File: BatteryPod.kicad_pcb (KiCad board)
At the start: 2 copper layers, 71.5 x 86.6 mm, 15 parts, among them J1 Conn_01x02_Pin, U1 LM5157RTER

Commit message: feat: almost full initial routing
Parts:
- added C8: 100uF, Capacitor_SMD:CP_Elec_16x17.5, F.Cu at (112.2, 125.7)
- added H1: MountingHole, MountingHole:MountingHole_2.5mm, B.Cu at (84.5, 103.5)
- added H2: MountingHole, MountingHole:MountingHole_2.5mm, B.Cu at (133.2, 100.4)
- added H3: MountingHole, MountingHole:MountingHole_2.5mm, B.Cu at (81.3, 141.9)
- added H4: MountingHole, MountingHole:MountingHole_2.5mm, B.Cu at (140.4, 142.0)
- C2: footprint Capacitor_SMD:C_0603_1608Metric -> Capacitor_SMD:C_2220_5750Metric
- J1: value Conn_01x02_Pin -> VIN; footprint Connector_PinHeader_2.54mm:PinHeader_1x02_P2.54mm_Vertical -> Connector_Wire:SolderWire-1.5sqmm_1x02_P7.8mm_D1.7mm_OD3.9mm
- moved R4 71.7 mm to (110.2, 79.9)
- moved R3 68.8 mm to (116.8, 81.4), turned to 180 degrees
- moved C6 64.6 mm to (113.1, 79.9), turned to 180 degrees
- moved C7 63.1 mm to (111.3, 83.7), turned to 180 degrees
- moved C5 60.7 mm to (113.1, 81.4), turned to 180 degrees
- moved U1 55.1 mm to (115.0, 84.3), turned to 180 degrees
- moved C3 54.4 mm to (118.7, 84.2), turned to 180 degrees
- moved R2 54.4 mm to (110.2, 82.2)
- moved J1 52.6 mm to (98.0, 82.0), turned to 135 degrees
- moved C2 51.2 mm to (91.5, 83.4), turned to 135 degrees
- moved R1 51.2 mm to (107.2, 82.2)
- moved C4 50.9 mm to (123.5, 92.4)
- moved D1 47.0 mm to (117.0, 89.8), turned to 180 degrees
- moved C1 41.9 mm to (122.0, 96.1)
- moved L1 11.4 mm to (104.0, 103.4), turned to 180 degrees
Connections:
- net Net-(D1-K) renamed VCC
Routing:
- net +BATT: track 0.00 -> 29.4 mm, vias 0 -> 1
- net VCC: track 0.00 -> 12.0 mm, vias 0 -> 2
- net /FB: track 0.00 -> 6.05 mm
- net Net-(U1-COMP): track 0.00 -> 3.04 mm
- net Net-(U1-SS): track 0.00 -> 1.76 mm
- net Net-(U1-VCC): track 0.00 -> 1.56 mm
- net Net-(U1-RT): track 0.00 -> 1.51 mm
- net Net-(C6-Pad2): track 0.00 -> 1.38 mm
- net GND: vias 0 -> 105
- added copper zone on F.Cu, net +BATT
- added copper zone on F.Cu, net /SW
- added copper zone on B.Cu, net GND
- added copper zone on F.Cu, net GND
- added copper zone on F.Cu, net VCC
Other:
- outline, holes or cut-outs redrawn
- board text added: "JLCJLCJLCJLC"

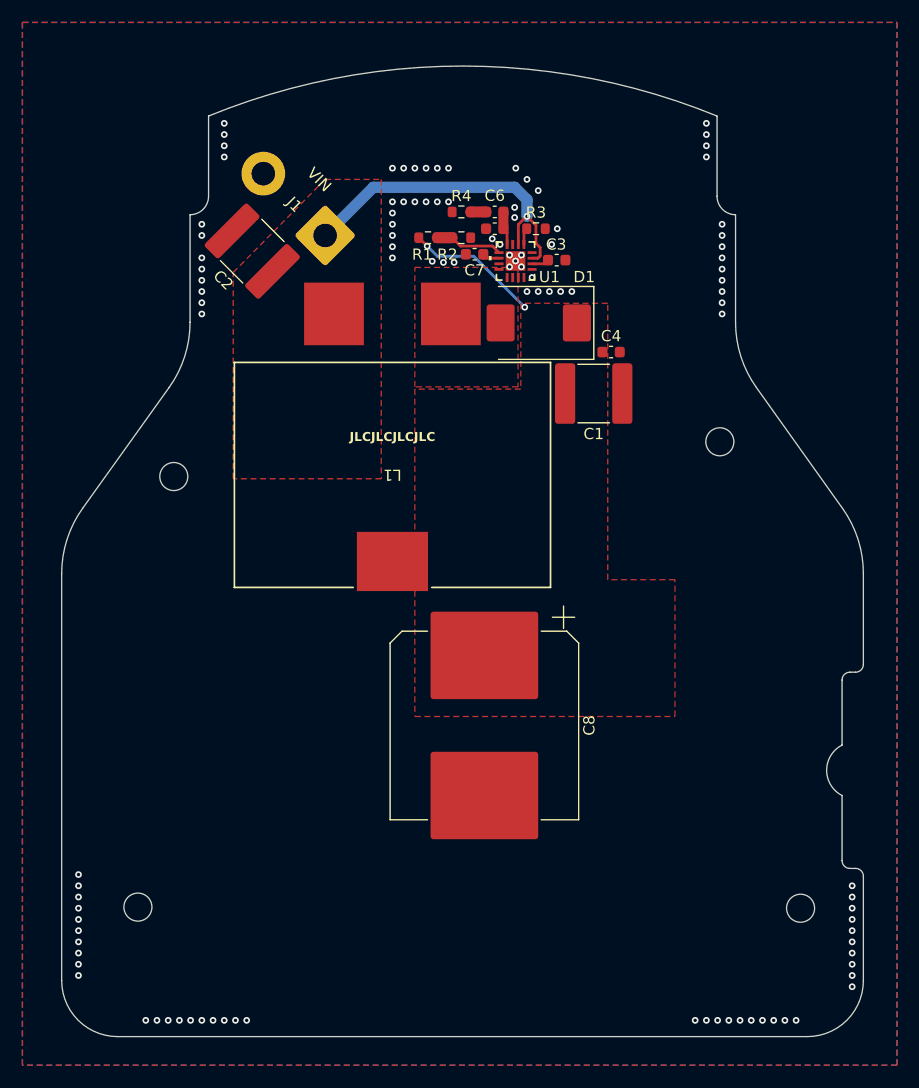
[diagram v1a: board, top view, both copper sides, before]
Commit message: feat: correct screw positioning (hopefully)
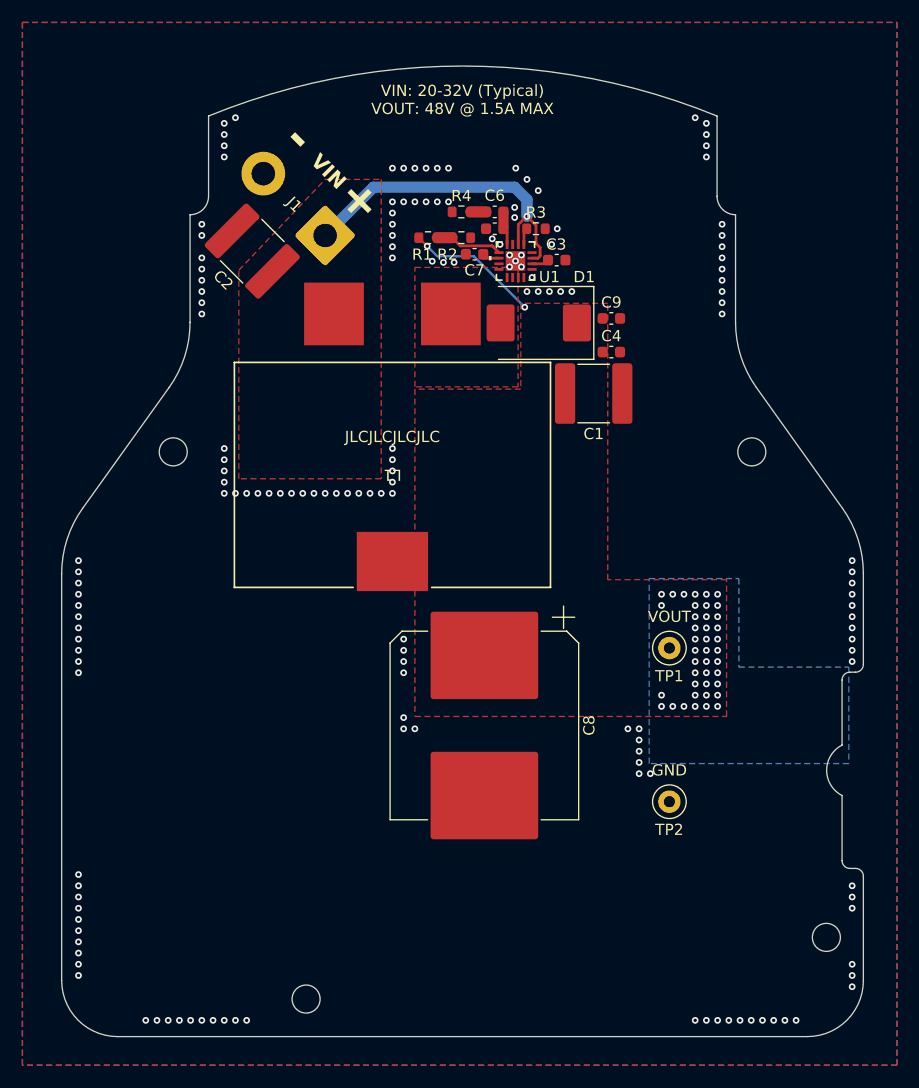
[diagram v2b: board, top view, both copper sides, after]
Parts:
- added C9: 0.1uF, Capacitor_SMD:C_0603_1608Metric, F.Cu at (123.5, 89.4)
- added TP1: VOUT, TestPoint:TestPoint_Loop_D2.50mm_Drill1.0mm_LowProfile, F.Cu at (128.7, 118.8)
- added TP2: GND, TestPoint:TestPoint_Loop_D2.50mm_Drill1.0mm_LowProfile, F.Cu at (128.7, 132.5)
- moved H3 17.1 mm to (96.3, 150.1)
- moved H4 3.47 mm to (142.7, 144.6)
- moved H2 2.99 mm to (136.1, 101.3)
- moved H1 2.20 mm to (84.5, 101.3)
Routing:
- net VCC: vias 2 -> 43
- net GND: vias 105 -> 162
- added copper zone on B.Cu, net VCC
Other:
- board text added: "+"
- board text added: "-"
- board text added: "VIN: 20-32V (Typical) VOUT: 48V @ 1.5A MAX"

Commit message: patch: silkscreen improvements fix: screw hole position
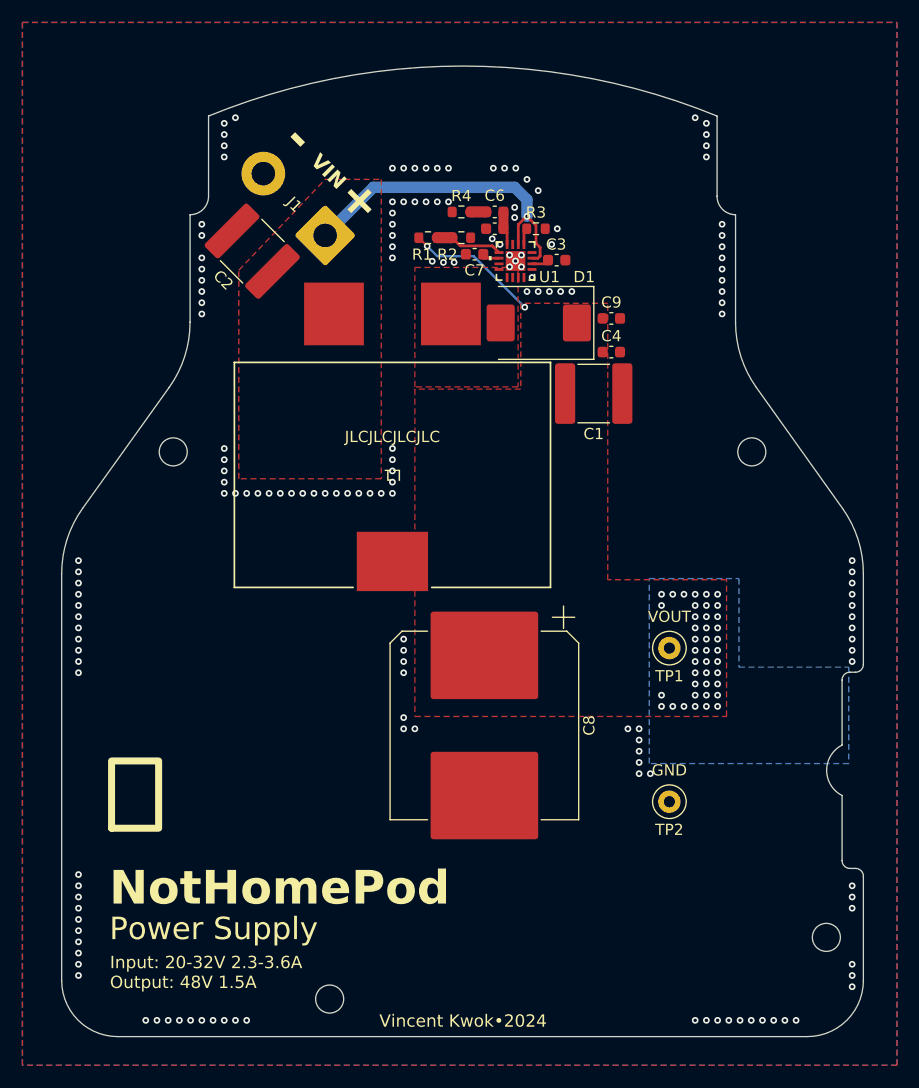
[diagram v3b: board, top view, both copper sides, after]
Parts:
- moved H3 2.10 mm to (98.4, 150.1)
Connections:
- L1 pad 3: (no net) -> unconnected-(L1-MOUNT-Pad3)
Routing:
- net GND: vias 162 -> 164
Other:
- board text added: "Input: 20-32V 2.3-3.6A Output: 48V 1.5A"
- board text added: "NotHomePod"
- board text added: "Power Supply"
- board text added: "Vincent Kwok•2024"
- board text added: "v0.1"
- board text added: "􀟣"
- board text removed: "VIN: 20-32V (Typical) VOUT: 48V @ 1.5A MAX"

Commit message: feat: add output pads
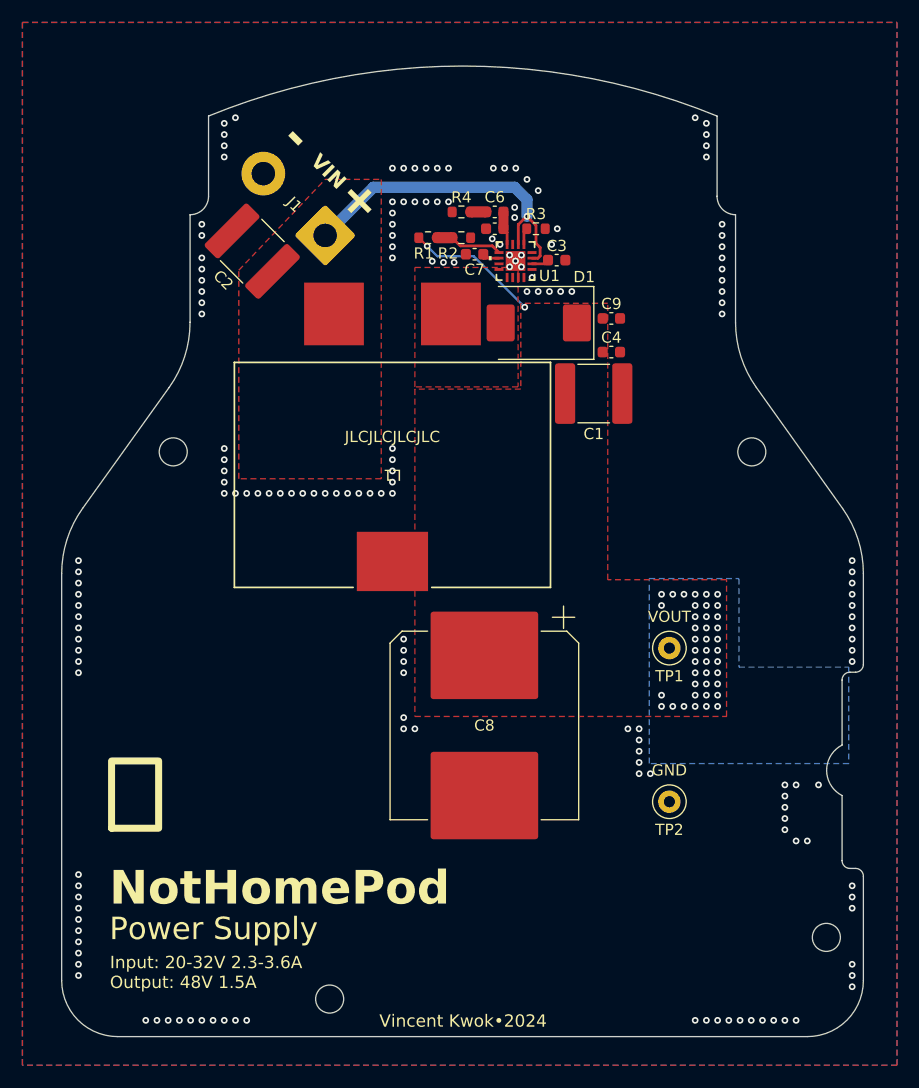
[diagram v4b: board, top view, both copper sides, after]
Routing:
- net GND: vias 164 -> 173
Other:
- board text added: "20-32V"
- board text added: "48V"
- board text added: "Input"
- board text added: "Output"

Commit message: feat: move to lower half of board due to high profile inductor this is to match with a recess in the chassis for the higher profile component
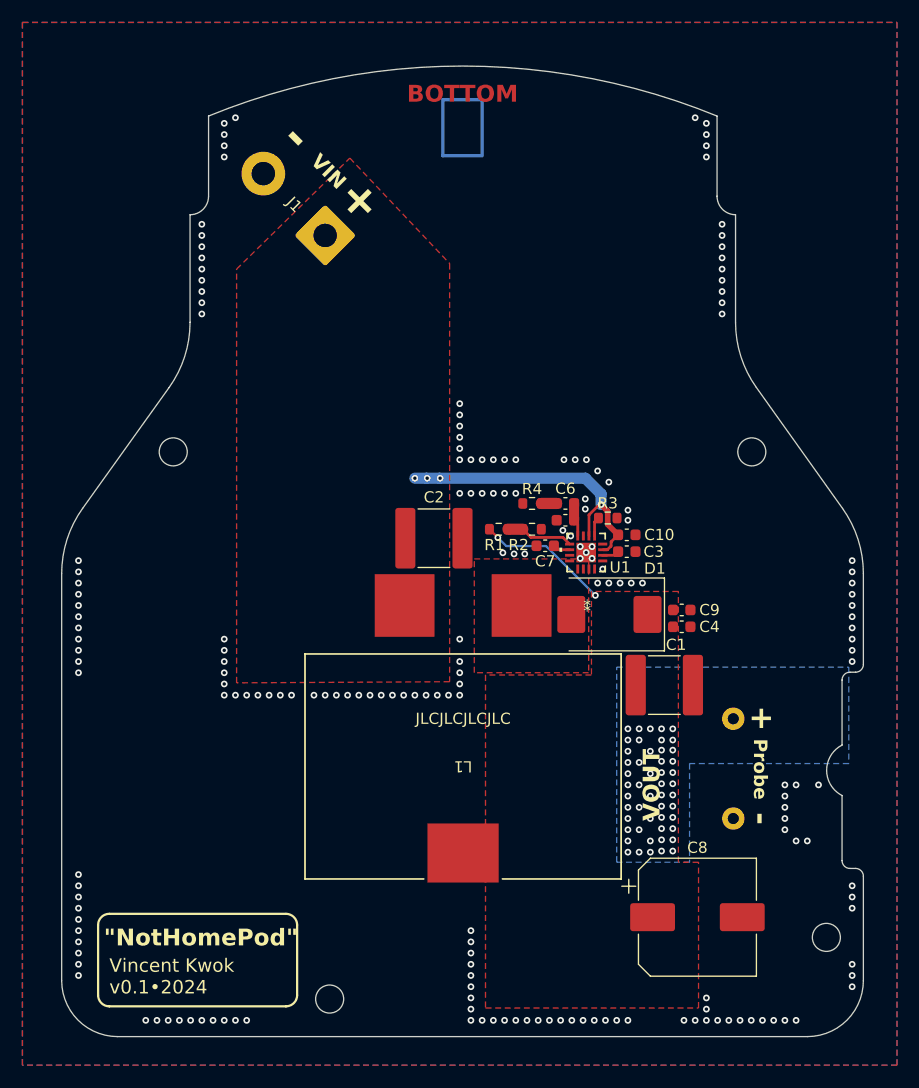
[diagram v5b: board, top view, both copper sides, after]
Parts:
- added C10: 0.1uF, Capacitor_SMD:C_0603_1608Metric, F.Cu at (124.9, 108.7)
- C8: footprint Capacitor_SMD:CP_Elec_16x17.5 -> Capacitor_SMD:CP_Elec_10x10
- TP1, TP2: moved to B.Cu
- moved C2 30.3 mm to (107.7, 109.0), turned to 0 degrees
- moved C1 26.8 mm to (128.2, 122.1)
- moved C5 26.8 mm to (119.4, 107.4)
- moved C6 26.8 mm to (119.4, 105.9)
- moved C7 26.8 mm to (117.6, 109.7)
- moved D1 26.8 mm to (123.3, 115.8)
- moved R1 26.8 mm to (113.5, 108.2)
- moved R2 26.8 mm to (116.5, 108.2)
- moved R4 26.8 mm to (116.5, 105.9)
- moved U1 26.8 mm to (121.3, 110.3)
- moved L1 26.8 mm to (110.3, 129.4)
- moved C9 26.7 mm to (129.8, 115.4)
- moved C3 26.7 mm to (124.9, 110.2)
- moved R3 26.6 mm to (123.2, 107.2)
- moved C8 25.6 mm to (131.2, 142.8), turned to 0 degrees
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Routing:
- net +BATT: track 29.4 -> 26.9 mm, vias 1 -> 4
- net VCC: track 12.0 -> 11.9 mm, vias 43 -> 52
- net GND: vias 173 -> 192
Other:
- board text added: "BOTTOM"
- board text added: "Probe"
- board text added: "VOUT"
- board text added: "Vincent Kwok v0.1•2024"
- board text added: "{dblquote}NotHomePod{dblquote}"
- board text added: "􀄿"
- board text removed: "Vincent Kwok•2024"
